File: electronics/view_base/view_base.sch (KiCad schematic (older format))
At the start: 92 parts, among them J1 BLDC, J2 USB_C_Receptacle_USB2.0, J3 LCD, J4 A, J5 B, Q1 MMBT4403, Q2 UMH3N, U1 MT6701-CT, U2 T-Micro32_Plus, U3 CH340C, U4 HX711, U5 TMC6300, U6 AP1117-33, U7 SN74LV1T34DBV, U8 VEML7700

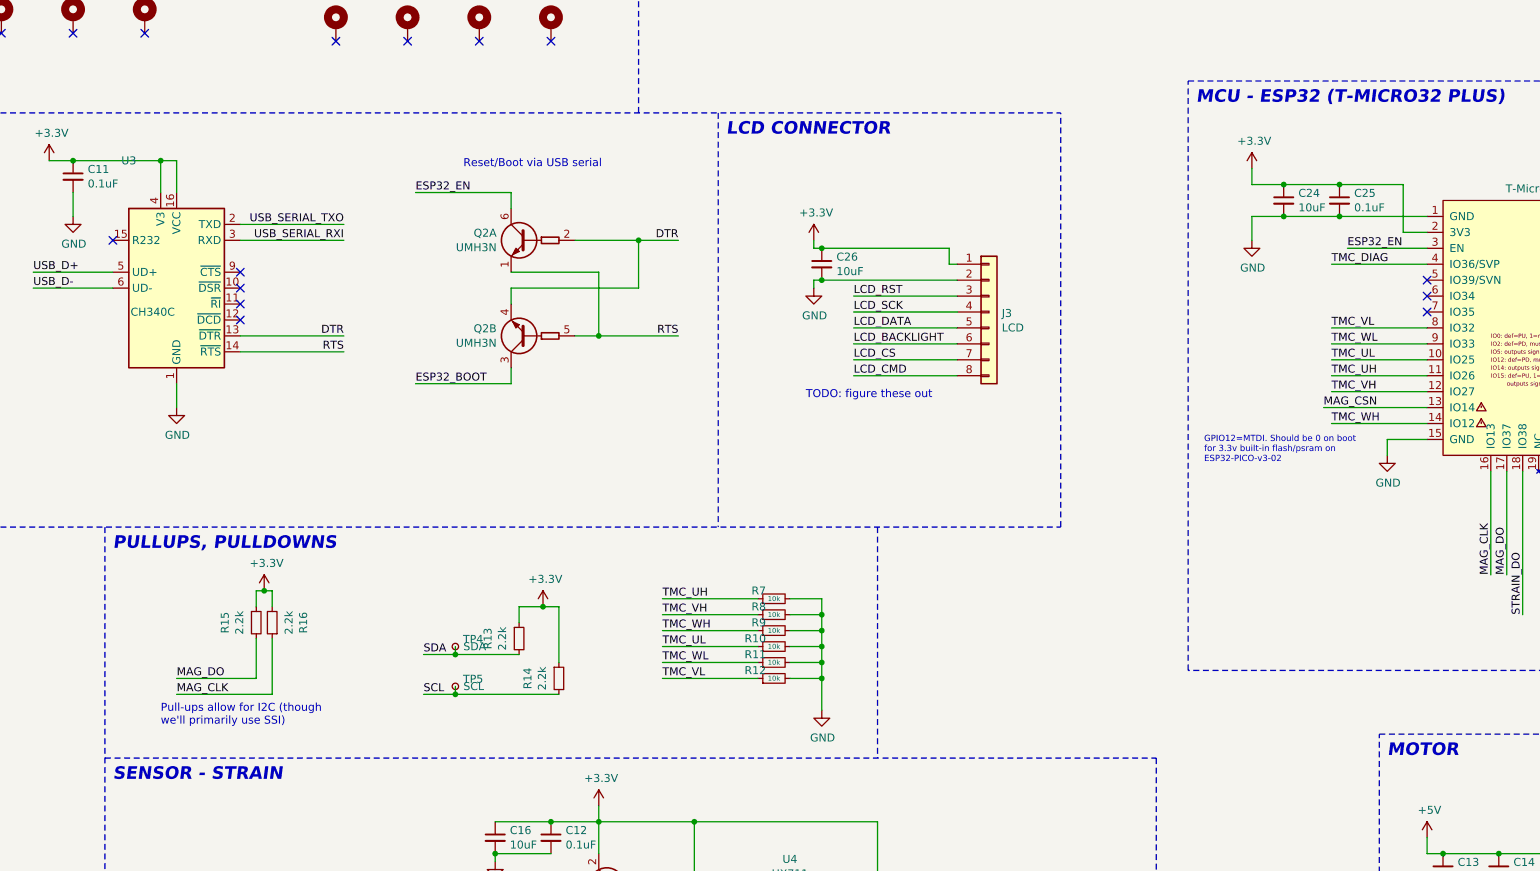
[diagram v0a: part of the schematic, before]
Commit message: Add EN pullup, capacitor, test points
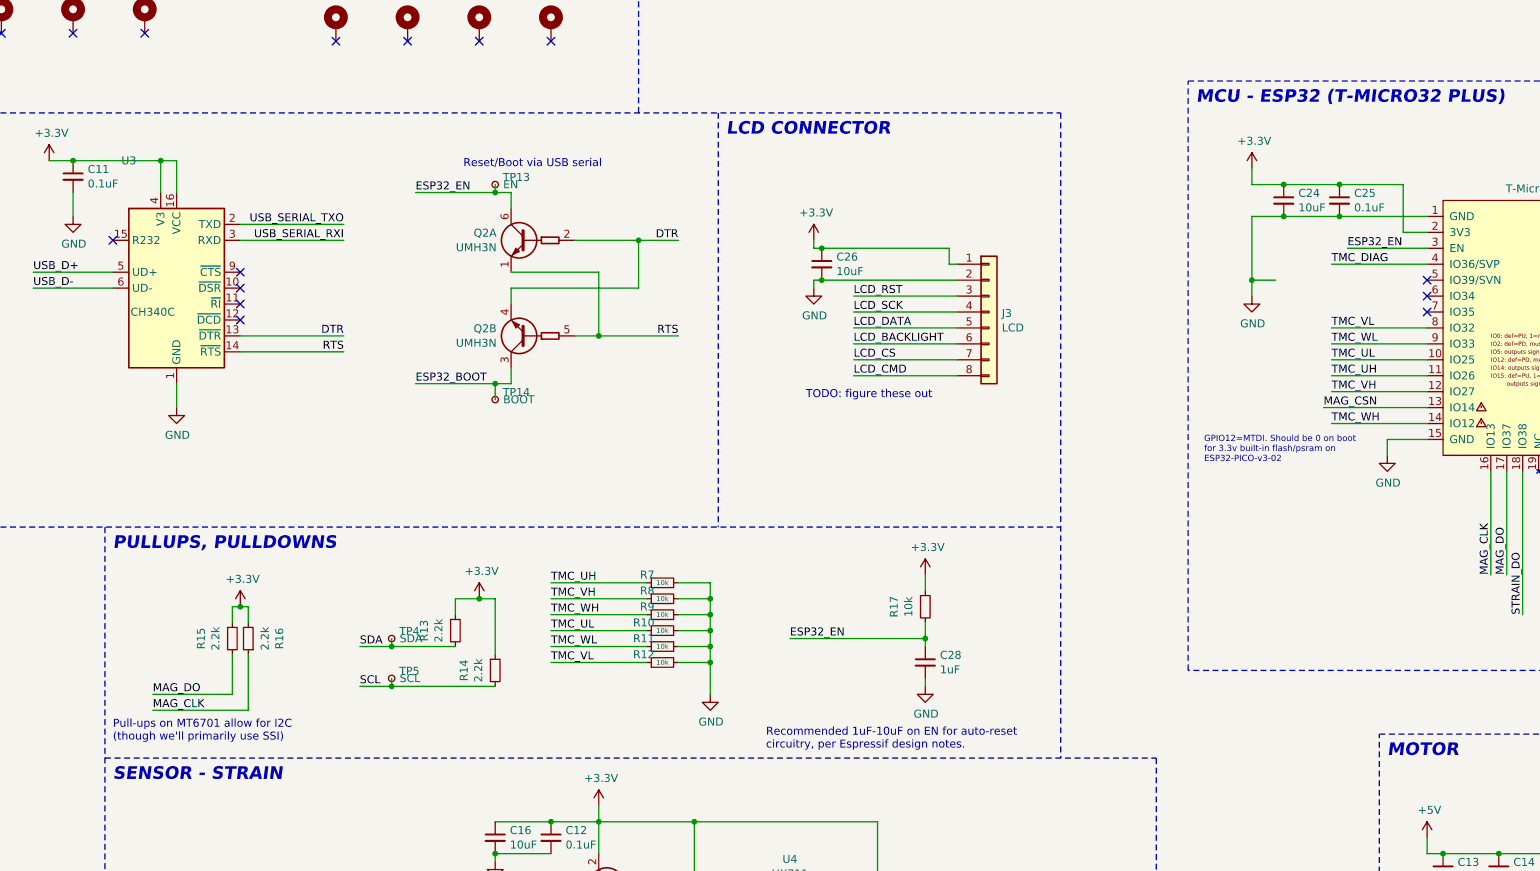
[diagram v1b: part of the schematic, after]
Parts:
- added C28: 1uF, Capacitor_SMD:C_0603_1608Metric, symbol Device:C_Small
- added R17: 10k, Resistor_SMD:R_0603_1608Metric, symbol Device:R_Small
- added TP13: EN, Modified:TestPoint_Pad_D2.0mm_ValueSilk, symbol Connector:TestPoint_Small
- added TP14: BOOT, Modified:TestPoint_Pad_D2.0mm_ValueSilk, symbol Connector:TestPoint_Small
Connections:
- wire segments 352 -> 363
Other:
- note added: "Pull-ups on MT6701 allow for I2C\n(though we'll primarily use SSI)"
- note added: "Recommended 1uF-10uF on EN for auto-reset\ncircuitry, per Espressif design notes."
- note removed: "Pull-ups allow for I2C (though\nwe'll primarily use SSI)"
- moved on the sheet: R10, R11, R12, R13, R14, R15, R16, R7, R8, R9, TP4, TP5

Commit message: Remove paste from USB-C pads
USB-C connector will be soldered separately from main top reflow, since it hangs below the board.
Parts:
- J2: footprint GCT_USB:USB4510 -> GCT_USB:USB4510_NoPaste
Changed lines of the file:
@@
 F 0 "J2" H 1607 3867 50  0000 C CNN
 F 1 "USB_C_Receptacle_USB2.0" H 1607 3776 50  0000 C CNN
-F 2 "GCT_USB:USB4510" H 1650 3000 50  0001 C CNN
+F 2 "GCT_USB:USB4510_NoPaste" H 1650 3000 50  0001 C CNN
 F 3 "https://www.usb.org/sites/default/files/documents/usb_type-c.zip" H 1650 3000 50  0001 C CNN
 	1    1500 3000

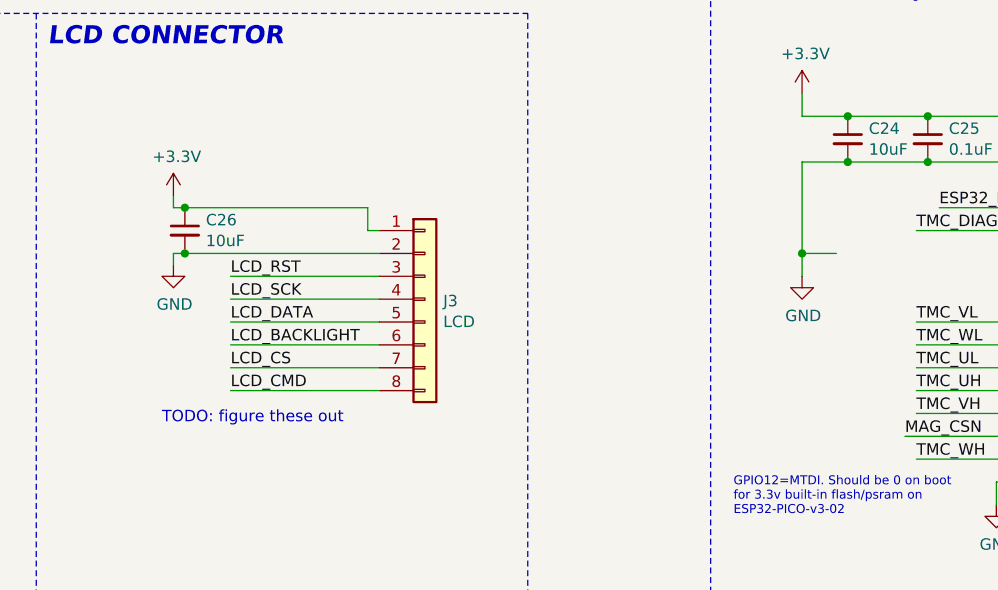
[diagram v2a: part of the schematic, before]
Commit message: Clean up schematic
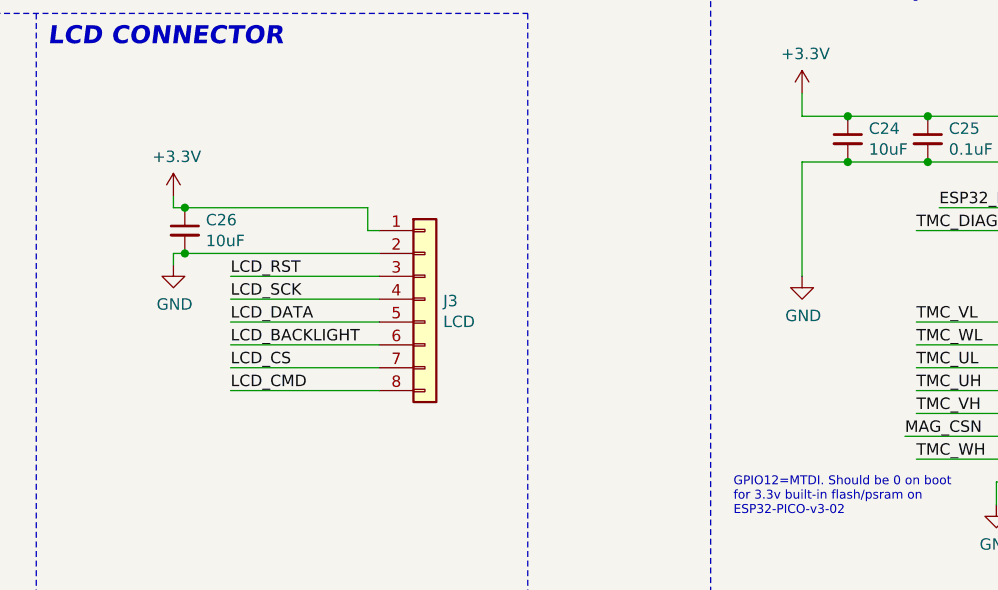
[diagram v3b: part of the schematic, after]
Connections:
- wire segments 363 -> 361
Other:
- note removed: "TODO: figure these out"
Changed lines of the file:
@@
 Text Label 9050 3600 0    50   ~ 0
 LCD_CMD
-Text Notes 8750 3750 0    50   ~ 0
-TODO: figure these out
 Wire Wire Line
 	7750 6800 7950 6800
@@
 Wire Notes Line
 	7700 1950 7700 500
-Wire Wire Line
-	11550 2600 11550 3000
 $Comp
 L Device:C_Small C28
@@
 	1    0    0    -1
 $EndComp
-Wire Wire Line
-	11700 3000 11550 3000
-Connection ~ 11550 3000
-Wire Wire Line
-	11550 3000 11550 3100
 Text Notes 8500 5950 0    50   ~ 0
 Recommended 1uF-10uF on EN for auto-reset\ncircuitry, per Espressif design notes.
@@
 Wire Wire Line
 	8650 5250 9500 5250
+Wire Wire Line
+	11550 2600 11550 3100
 $EndSCHEMATC

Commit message: Fix HX711 analog supply, fix 3.3v regulator
Fixes #8
Fixes #3
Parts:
- R3: value 20k -> 10k
- U6: value AP1117-33 -> AP2114HA-3.3; symbol Regulator_Linear:AP1117-33 -> Regulator_Linear:AP7361C-33E
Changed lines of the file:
@@
 $EndComp
 $Comp
-L Regulator_Linear:AP1117-33 U6
+L Regulator_Linear:AP7361C-33E U6
 U 1 1 6203D4F8
 P 1900 1150
 F 0 "U6" H 1900 1392 50  0000 C CNN
-F 1 "AP1117-33" H 1900 1301 50  0000 C CNN
+F 1 "AP2114HA-3.3" H 1900 1301 50  0000 C CNN
 F 2 "Package_TO_SOT_SMD:SOT-223-3_TabPin2" H 1900 1350 50  0001 C CNN
-F 3 "http://www.diodes.com/datasheets/AP1117.pdf" H 2000 900 50  0001 C CNN
+F 3 "" H 2000 900 50  0001 C CNN
 	1    1900 1150
 	1    0    0    -1
@@
 P 7250 7250
 F 0 "R3" H 7309 7296 50  0000 L CNN
-F 1 "20k" H 7309 7205 50  0000 L CNN
+F 1 "10k" H 7309 7205 50  0000 L CNN
 F 2 "Resistor_SMD:R_0603_1608Metric" H 7250 7250 50  0001 C CNN
 F 3 "~" H 7250 7250 50  0001 C CNN

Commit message: Add a bunch of part numbers to BOM
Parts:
- C1, C11, C12, C14, C15, C17, C19, C2, C20, C21, C22, C23, C25, C27, C29, C3, C4, C5, C6, C7, C8: Digikey (none) -> 1276-1935-1-ND; LCSC (none) -> C1591; Mouser (none) -> 187-CL10B104KB8NNWC
- C10, C16, C18, C24, C26, C9: Digikey (none) -> 1276-2891-1-ND; LCSC (none) -> C2922480; Mouser (none) -> 187-CL21A106KAYNNNE
- C13: Digikey (none) -> 1276-CL21A226MAYNNNECT-ND; LCSC (none) -> C98190; Mouser (none) -> 187-CL21A226MAYNNNE
- C28: Digikey (none) -> 1276-1102-1-ND; LCSC (none) -> C5673; Mouser (none) -> 187-CL10A105KA8NNNC
- D1, D2, D3, D4, D5, D6, D7, D8: AliExpress (none) -> https://www.aliexpress.com/item/10000009330139.html; Digikey (none) -> 1528-4691-ND; LCSC (none) -> C2890037; Mouser (none) -> 485-4691
- H1, H2, H3: Note (none) -> Screw: M1.6x10 (countersunk), or M1.6x9 (pan/round)
- H4, H5, H6, H7: footprint MountingHole:MountingHole_2.2mm_M2_ISO7380_Pad -> Holes:MountingHole_2.2mm_M2_ISO7380_Pad_NonVirtual; Note (none) -> Screw: M2x5 (pan/round); Nut: M2 hex
- J1: Digikey (none) -> WM7621CT-ND; LCSC (none) -> C293630; Mouser (none) -> 538-53261-0371
- J2: Digikey (none) -> USB4510-03-1-A; LCSC (none) -> C428463; Mouser (none) -> 640-USB4510031A
- L1: Digikey (none) -> 445-6394-1-ND; LCSC (none) -> C307744; Mouser (none) -> 810-MLZ2012A3R3WT000
- Q1: Digikey (none) -> MMBT4403LT1GOSCT-ND; LCSC (none) -> C78864; Mouser (none) -> 241-MMBT4403R100001
- Q2: Digikey (none) -> UMH3NTNCT-ND; LCSC (none) -> C62892; Mouser (none) -> 755-UMH3NTN
- R1, R2: Digikey (none) -> RMCF0603JT5K10CT-ND; LCSC (none) -> C105580; Mouser (none) -> 652-CR0603FX-5101ELF
- R10, R11, R12, R17, R3, R7, R8, R9: Digikey (none) -> RMCF0603JT10K0CT-ND; LCSC (none) -> C98220; Mouser (none) -> 652-CR0603FX-1002ELF
- R13, R14, R15, R16: Digikey (none) -> RMCF0603FT2K20CT-ND; LCSC (none) -> C4190; Mouser (none) -> 652-CR0603FX-2201ELF
- R4: Digikey (none) -> RMCF0603FT8K20CT-ND; LCSC (none) -> C114637; Mouser (none) -> 652-CR0603FX-8201ELF
- R5, R6: Digikey (none) -> RMCF0603FT100RCT-ND; LCSC (none) -> C319953; Mouser (none) -> 652-CR0603FX-1000ELF
- U1: Digikey (none) -> N/A; LCSC (none) -> C2856764; Mouser (none) -> N/A
- U2: AliExpress (none) -> https://www.aliexpress.com/item/1005002308952882.html; Digikey (none) -> N/A; LCSC (none) -> N/A; Mouser (none) -> N/A
- U3: Digikey (none) -> N/A; LCSC (none) -> C84681; Mouser (none) -> N/A
- U4: Digikey (none) -> N/A; LCSC (none) -> C43656; Mouser (none) -> N/A
- U5: Digikey (none) -> TMC6300-LA-T; LCSC (none) -> N/A; Mouser (none) -> 700-TMC6300-LA
- U6: Digikey (none) -> AP2114HA-3.3TRG1DICT-ND; LCSC (none) -> C460314; Mouser (none) -> 621-AP2114HA-3.3TRG1
- U7: Digikey (none) -> 296-37176-1-ND; LCSC (none) -> C100024; Mouser (none) -> 595-SN74LV1T34DBVR
- U8: Digikey (none) -> VEML7700-TT; LCSC (none) -> C1850416; Mouser (none) -> 78-VEML7700-TT
- Z1, Z2, Z3, Z4: value strain -> BF350-3AA Strain Gauge; AliExpress (none) -> https://www.aliexpress.com/item/4000204288561.html; Digikey (none) -> N/A; LCSC (none) -> N/A; Mouser (none) -> N/A
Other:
- note added: "MECHANICAL/BOM-ONLY"
- note added: "MOTOR DRIVER"
- note removed: "MECHANICAL"
- note removed: "MOTOR"
- moved on the sheet: C24, C25, C27, H1, H2, H3, H4, H5, H6, H7, U2, U8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

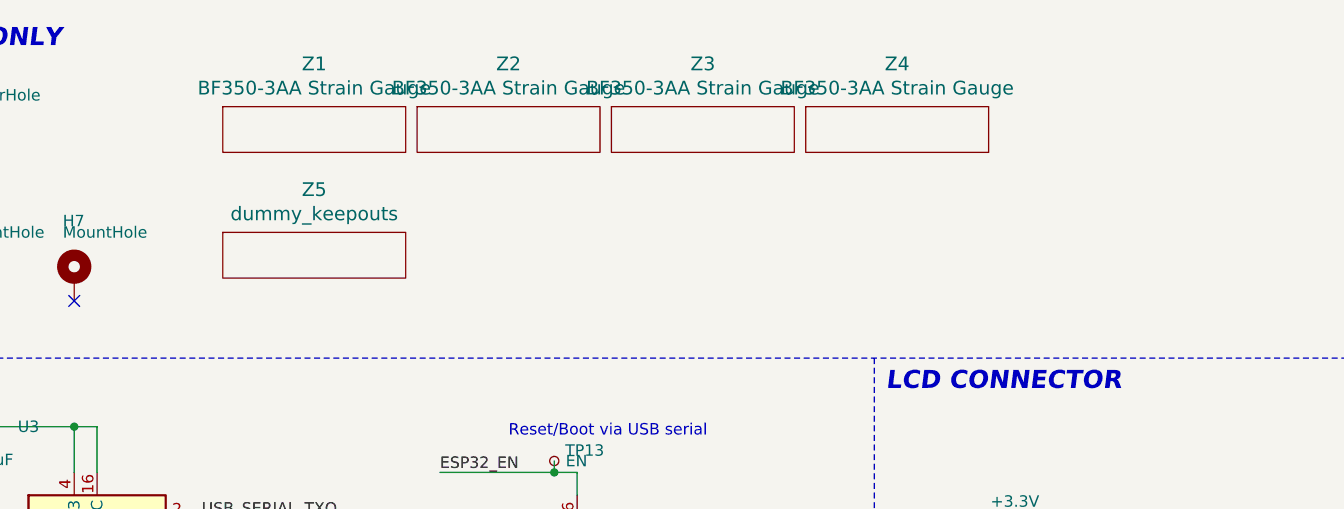
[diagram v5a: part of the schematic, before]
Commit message: Generate merged BOM (#15)
Also add more bom-only items to the schematic
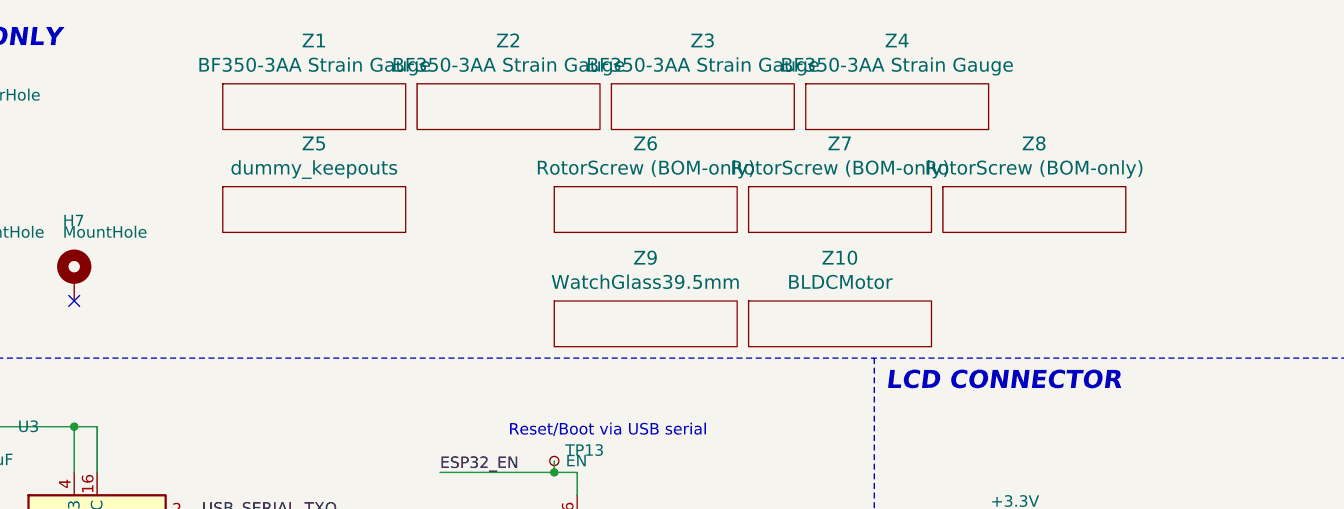
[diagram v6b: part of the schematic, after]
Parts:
- added Z10: BLDCMotor, BOM_Only:bom_only_no_pin, symbol no_pin:no_pin
- added Z6, Z7, Z8: RotorScrew (BOM-only), BOM_Only:bom_only_no_pin, symbol no_pin:no_pin
- added Z9: WatchGlass39.5mm, BOM_Only:bom_only_no_pin, symbol no_pin:no_pin
- C1, C11, C12, C14, C15, C17, C19, C2, C20, C21, C22, C23, C25, C27, C29, C3, C4, C5, C6, C7, C8: Mouser 187-CL10B104KB8NNWC -> 187-CL10B104KB8NNWC
- C13: Mouser 187-CL21A226MAYNNNE -> 187-CL21A226MAYNNNE
- D1, D2, D3, D4, D5, D6, D7, D8: Mouser 485-4691 -> 485-4691
- U6: Mouser 621-AP2114HA-3.3TRG1 -> 621-AP2114HA-3.3TRG1
- U7: Mouser 595-SN74LV1T34DBVR -> 595-SN74LV1T34DBVR
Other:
- moved on the sheet: Z1, Z2, Z3, Z4, Z5

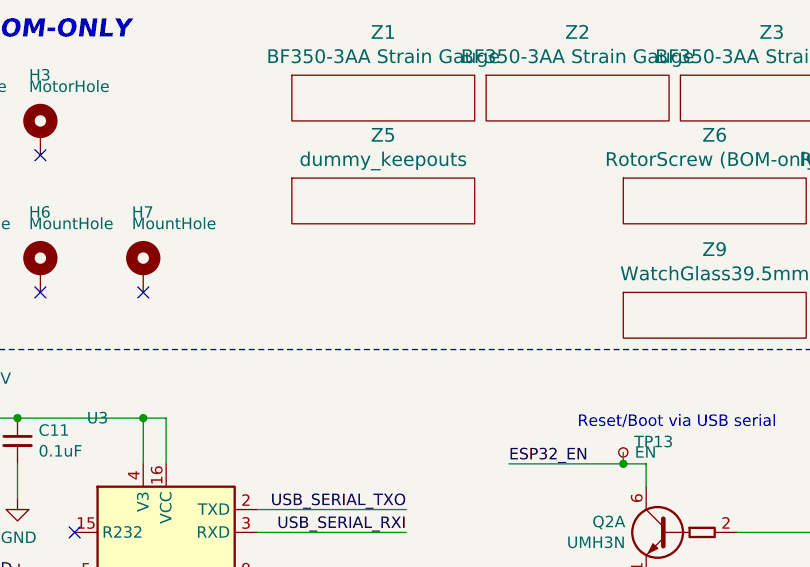
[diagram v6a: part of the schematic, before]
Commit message: Add alignment holes, update board outline - shorter slots
Fixes #7
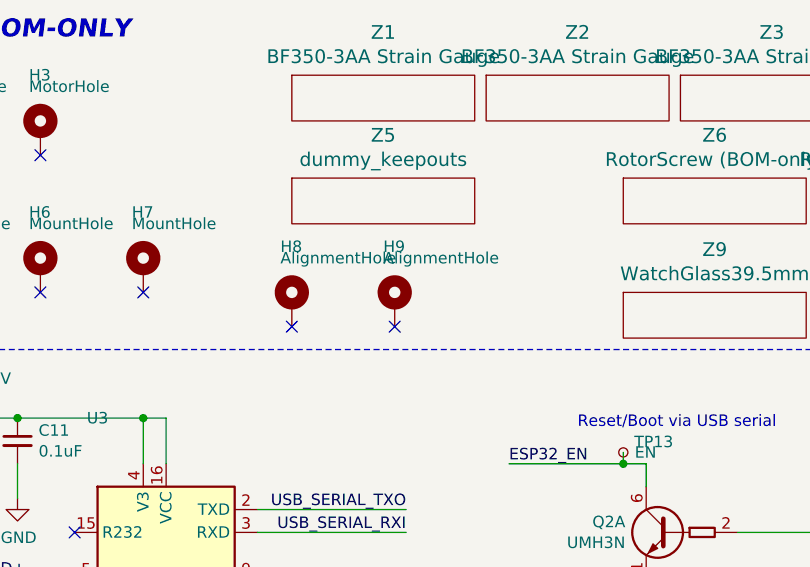
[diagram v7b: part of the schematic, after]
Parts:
- added H8, H9: AlignmentHole, Holes:MountingHole_2.2mm_M2_ISO7380_Pad_NonVirtual, symbol Mechanical:MountingHole_Pad
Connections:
- no-connect marks 22 -> 24
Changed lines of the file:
@@
 	1    0    0    -1
 $EndComp
+$Comp
+L Mechanical:MountingHole_Pad H8
+U 1 1 623284D1
+P 5350 1750
+F 0 "H8" H 5300 2000 50  0000 L CNN
+F 1 "AlignmentHole" H 5300 1950 50  0000 L CNN
+F 2 "Holes:MountingHole_2.2mm_M2_ISO7380_Pad_NonVirtual" H 5350 1750 50  0001 C CNN
+F 3 "~" H 5350 1750 50  0001 C CNN
+F 4 "" H 5350 1750 50  0001 C CNN "Note"
+	1    5350 1750
+	1    0    0    -1
+$EndComp
+NoConn ~ 5350 1850
+$Comp
+L Mechanical:MountingHole_Pad H9
+U 1 1 623284D9
+P 5800 1750
+F 0 "H9" H 5750 2000 50  0000 L CNN
+F 1 "AlignmentHole" H 5750 1950 50  0000 L CNN
+F 2 "Holes:MountingHole_2.2mm_M2_ISO7380_Pad_NonVirtual" H 5800 1750 50  0001 C CNN
+F 3 "~" H 5800 1750 50  0001 C CNN
+F 4 "" H 5800 1750 50  0001 C CNN "Note"
+	1    5800 1750
+	1    0    0    -1
+$EndComp
+NoConn ~ 5800 1850
 $EndSCHEMATC
